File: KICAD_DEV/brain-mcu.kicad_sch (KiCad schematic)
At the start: 5 parts, among them U1 STM32H757IITx

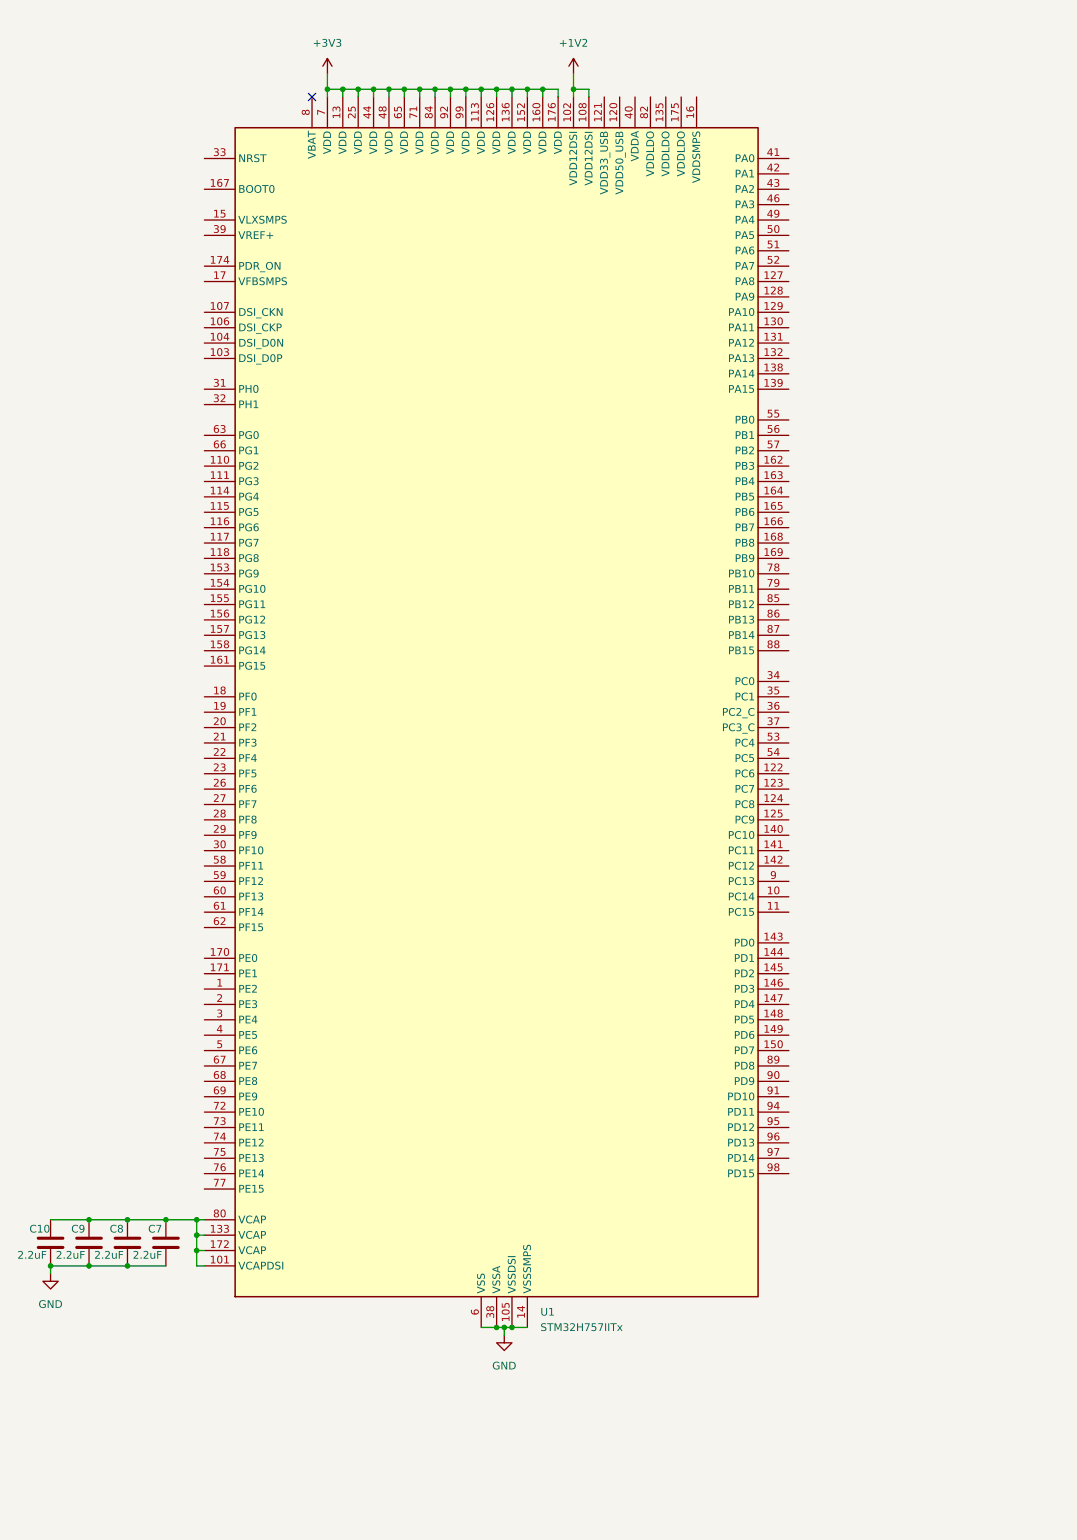
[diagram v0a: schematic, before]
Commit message: some decoupling and organization
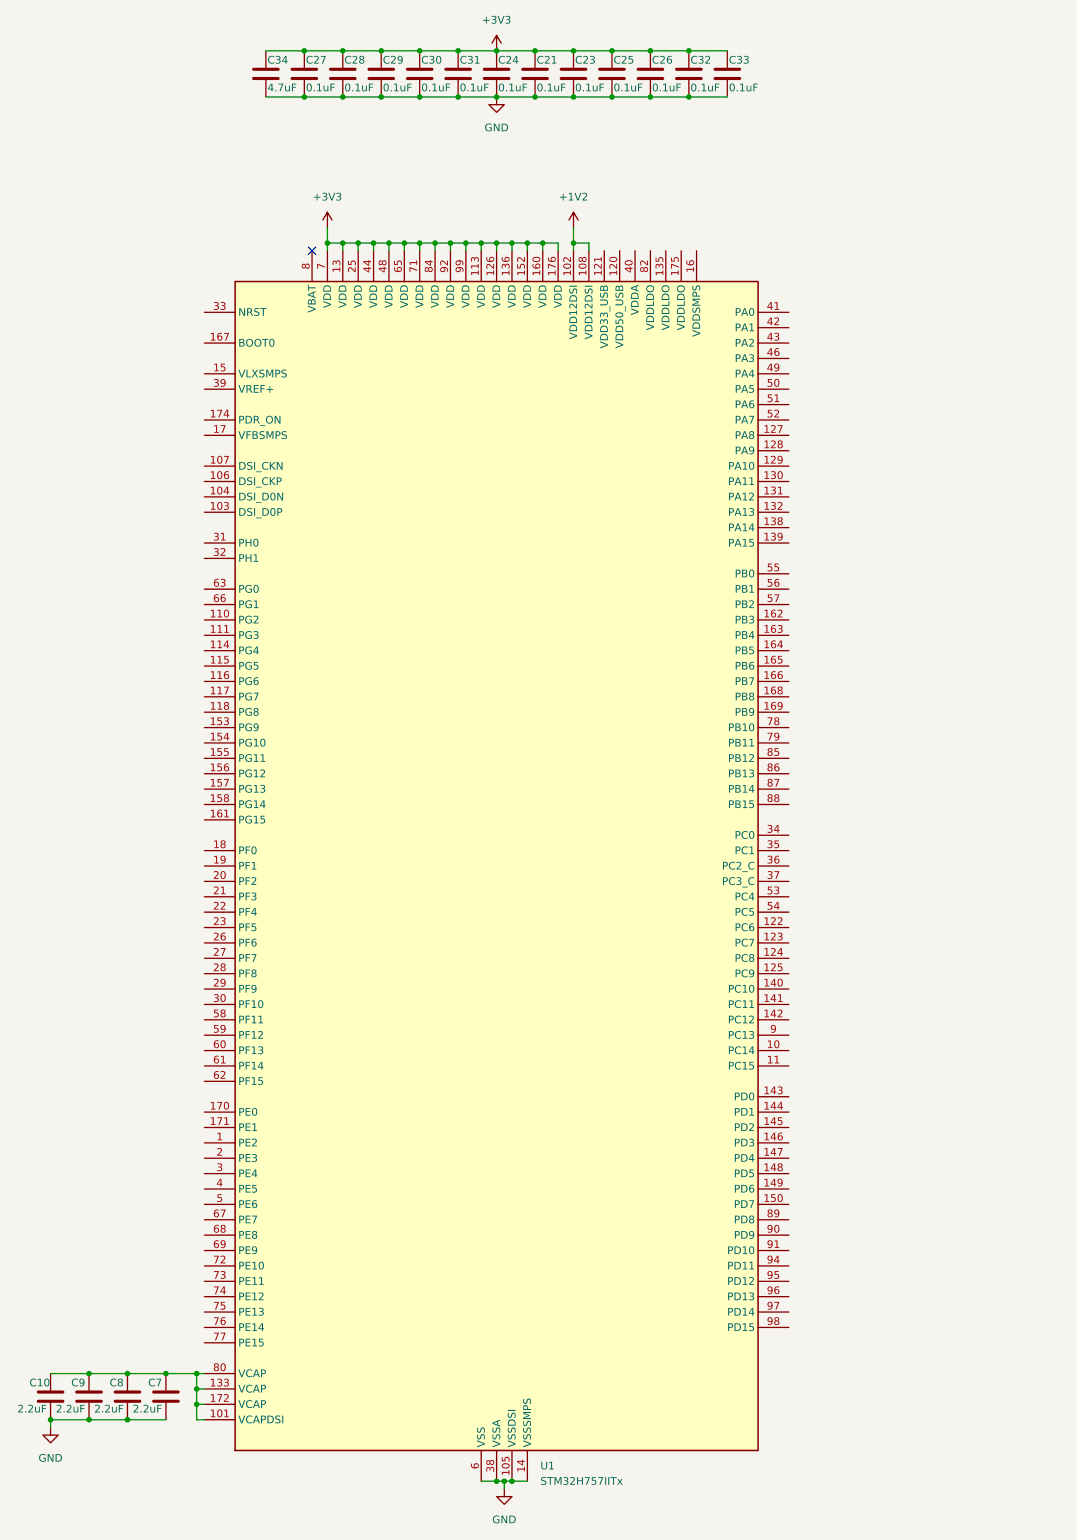
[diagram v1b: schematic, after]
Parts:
- added C21, C23, C24, C25, C26, C27, C28, C29, C30, C31, C32, C33: 0.1uF, symbol Device:C
- added C34: 4.7uF, symbol Device:C
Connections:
- net +3V3: now also C21.1, C23.1, C24.1, C25.1, C26.1, C27.1, C28.1, C29.1, C30.1, C31.1, C32.1, C33.1, C34.1
- net GND: now also C21.2, C23.2, C24.2, C25.2, C26.2, C27.2, C28.2, C29.2, C30.2, C31.2, C32.2, C33.2, C34.2
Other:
- moved on the sheet: C10, C7, C8, C9, U1

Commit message: changing the MCU for more chaos
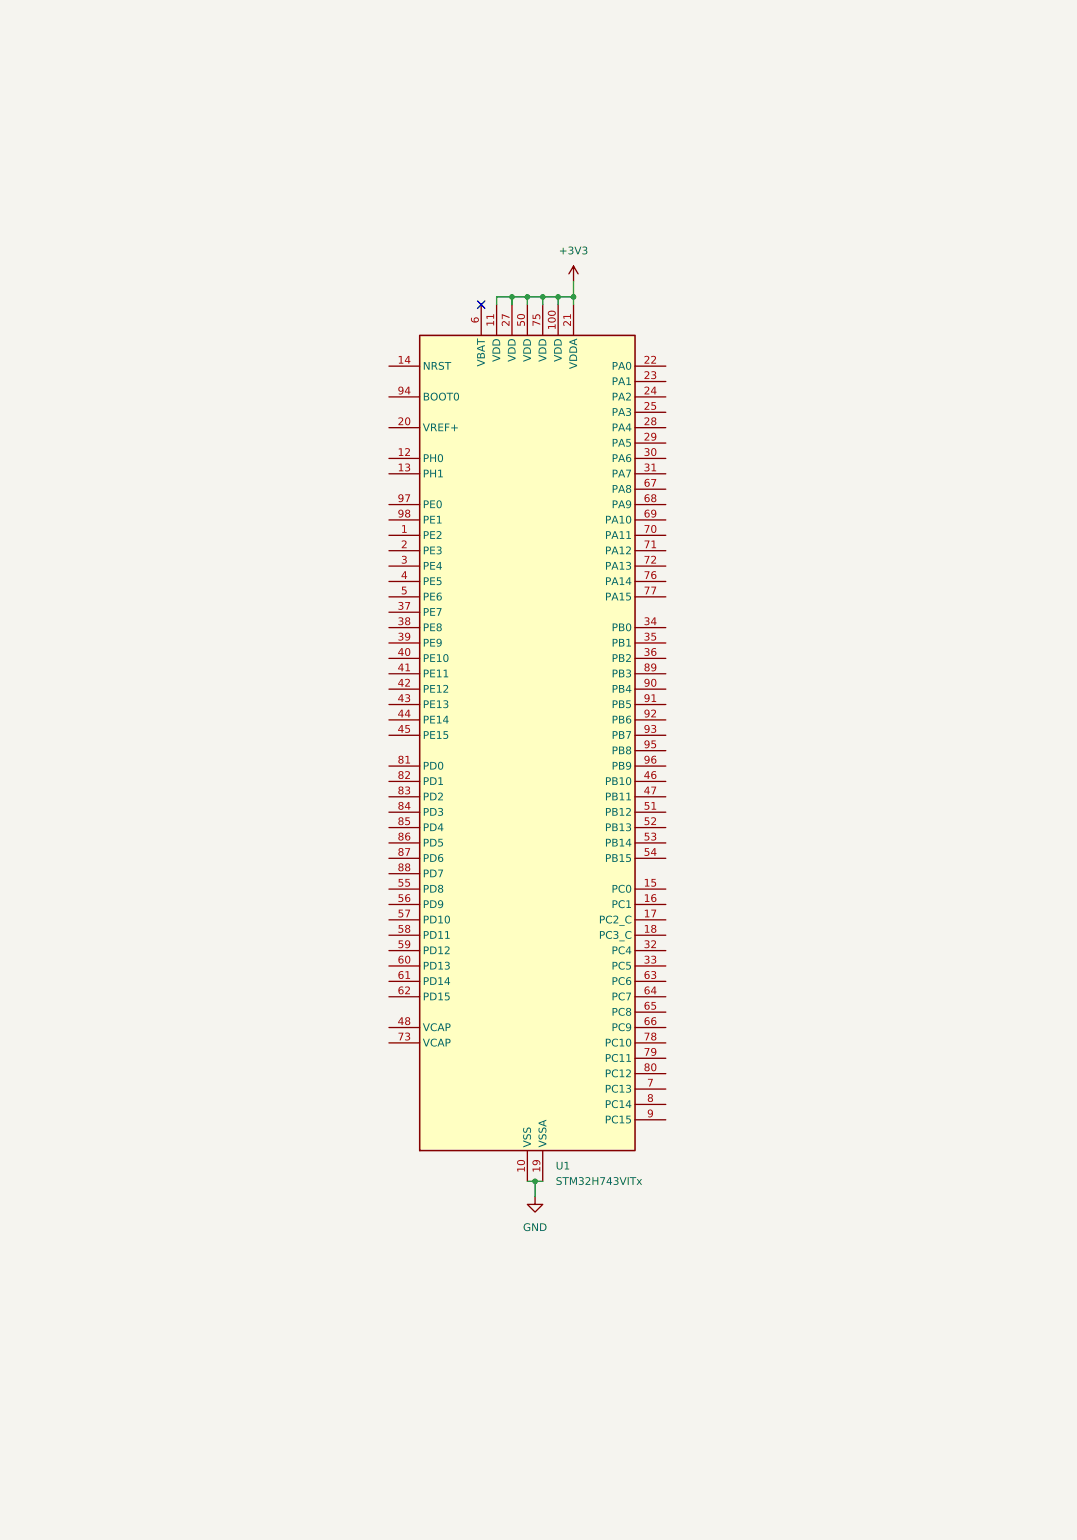
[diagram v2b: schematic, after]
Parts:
- removed C10, C7, C8, C9: 2.2uF, symbol Device:C
- removed C21, C23, C24, C25, C26, C27, C28, C29, C30, C31, C32, C33: 0.1uF, symbol Device:C
- removed C34: 4.7uF, symbol Device:C
- removed U1: STM32H757IITx, Package_QFP:LQFP-176_24x24mm_P0.5mm, symbol MCU_ST_STM32H7:STM32H757IITx
- added U1: STM32H743VITx, Package_QFP:LQFP-100_14x14mm_P0.5mm, symbol MCU_ST_STM32H7:STM32H743VITx
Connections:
- net +3V3: now also U1.100 (VDD), U1.11 (VDD), U1.21 (VDDA), U1.27 (VDD), U1.50 (VDD), U1.75 (VDD)
- net GND: now also U1.10 (VSS), U1.19 (VSSA), U1.26 (VSS), U1.49 (VSS), U1.74 (VSS), U1.99 (VSS)

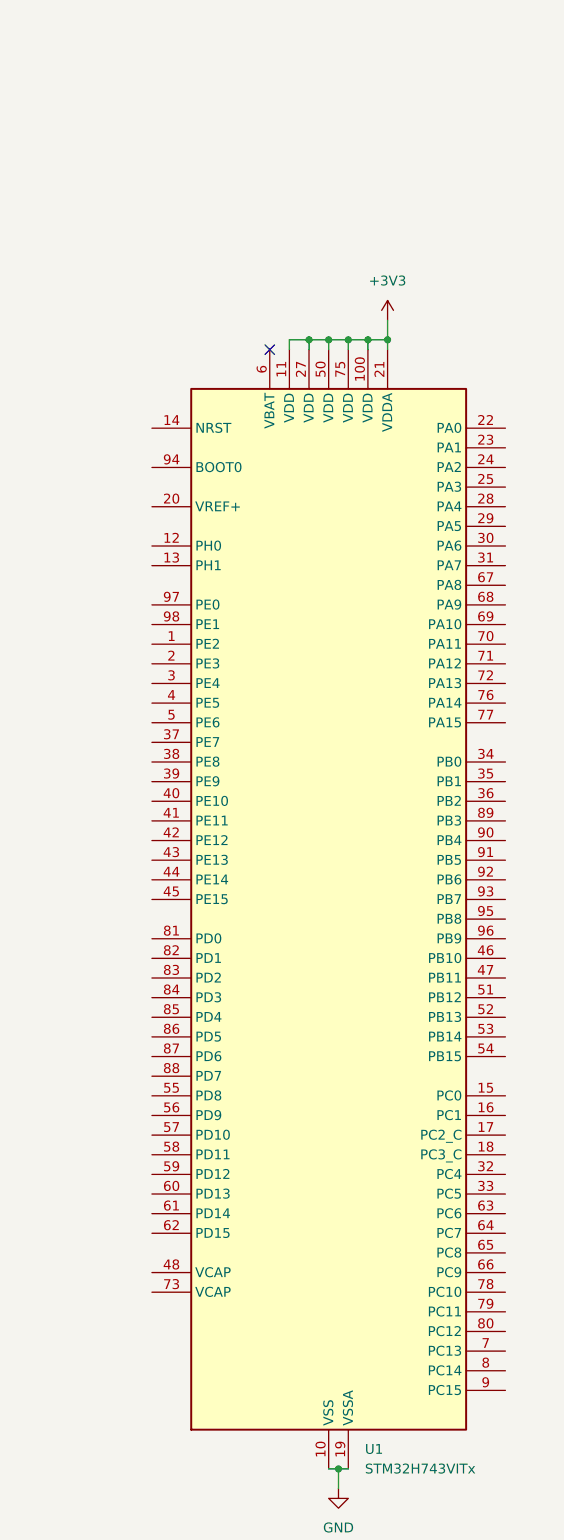
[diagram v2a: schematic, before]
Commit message: decoupling caps, vref, and vcap
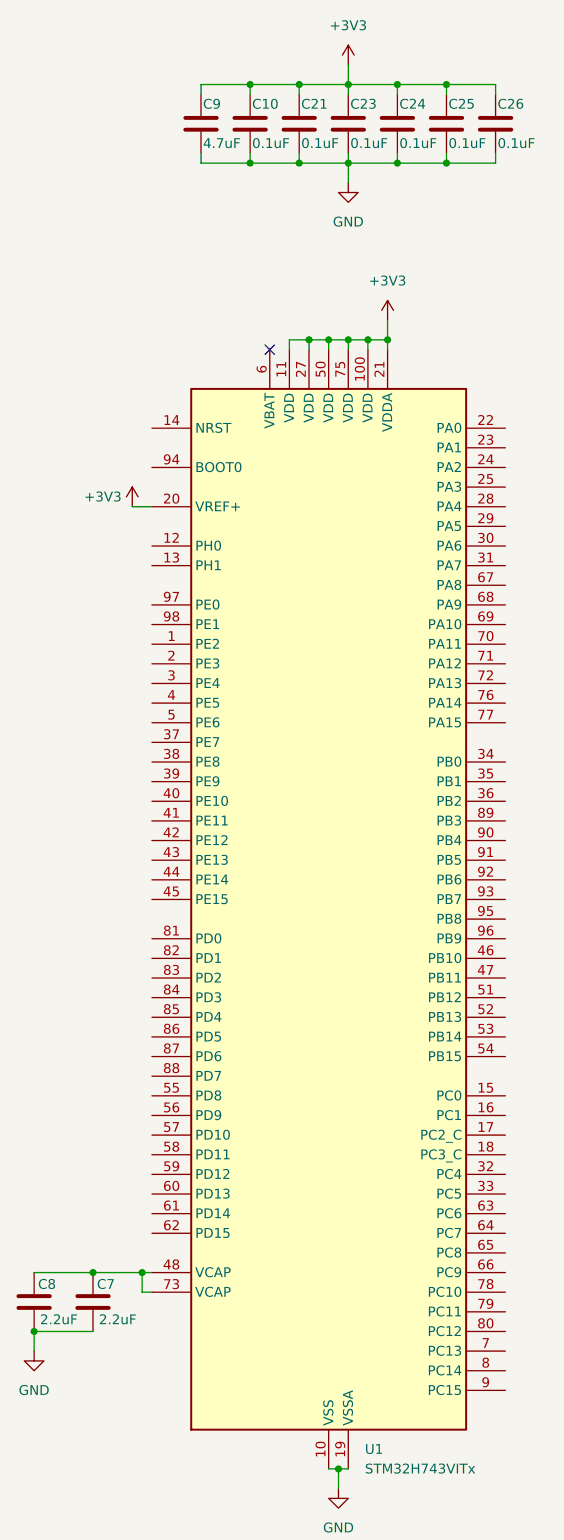
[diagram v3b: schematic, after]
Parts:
- added C10, C21, C23, C24, C25, C26: 0.1uF, symbol Device:C
- added C7, C8: 2.2uF, symbol Device:C
- added C9: 4.7uF, symbol Device:C
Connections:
- net +3V3: now also U1.20 (VREF+), C10.1, C21.1, C23.1, C24.1, C25.1, C26.1, C9.1
- net GND: now also C10.2, C21.2, C23.2, C24.2, C25.2, C26.2, C7.2, C8.2, C9.2
- net at U1.48 (VCAP): now also U1.73 (VCAP), C7.1, C8.1

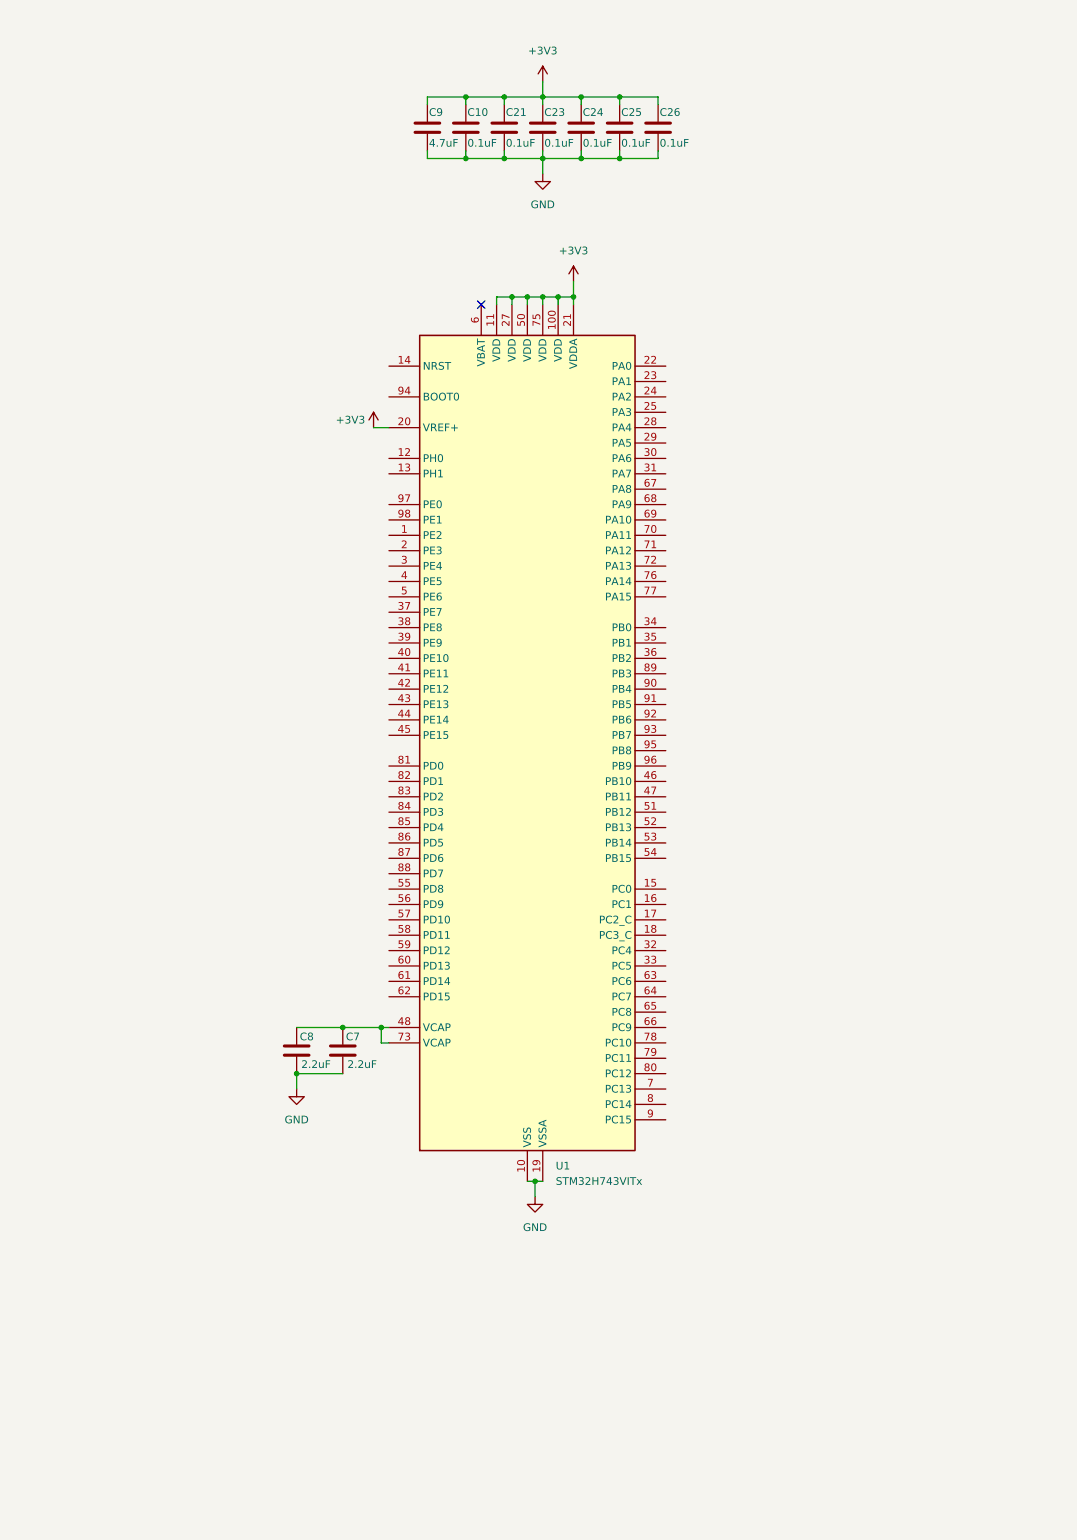
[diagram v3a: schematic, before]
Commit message: NRST and cleaner schematic
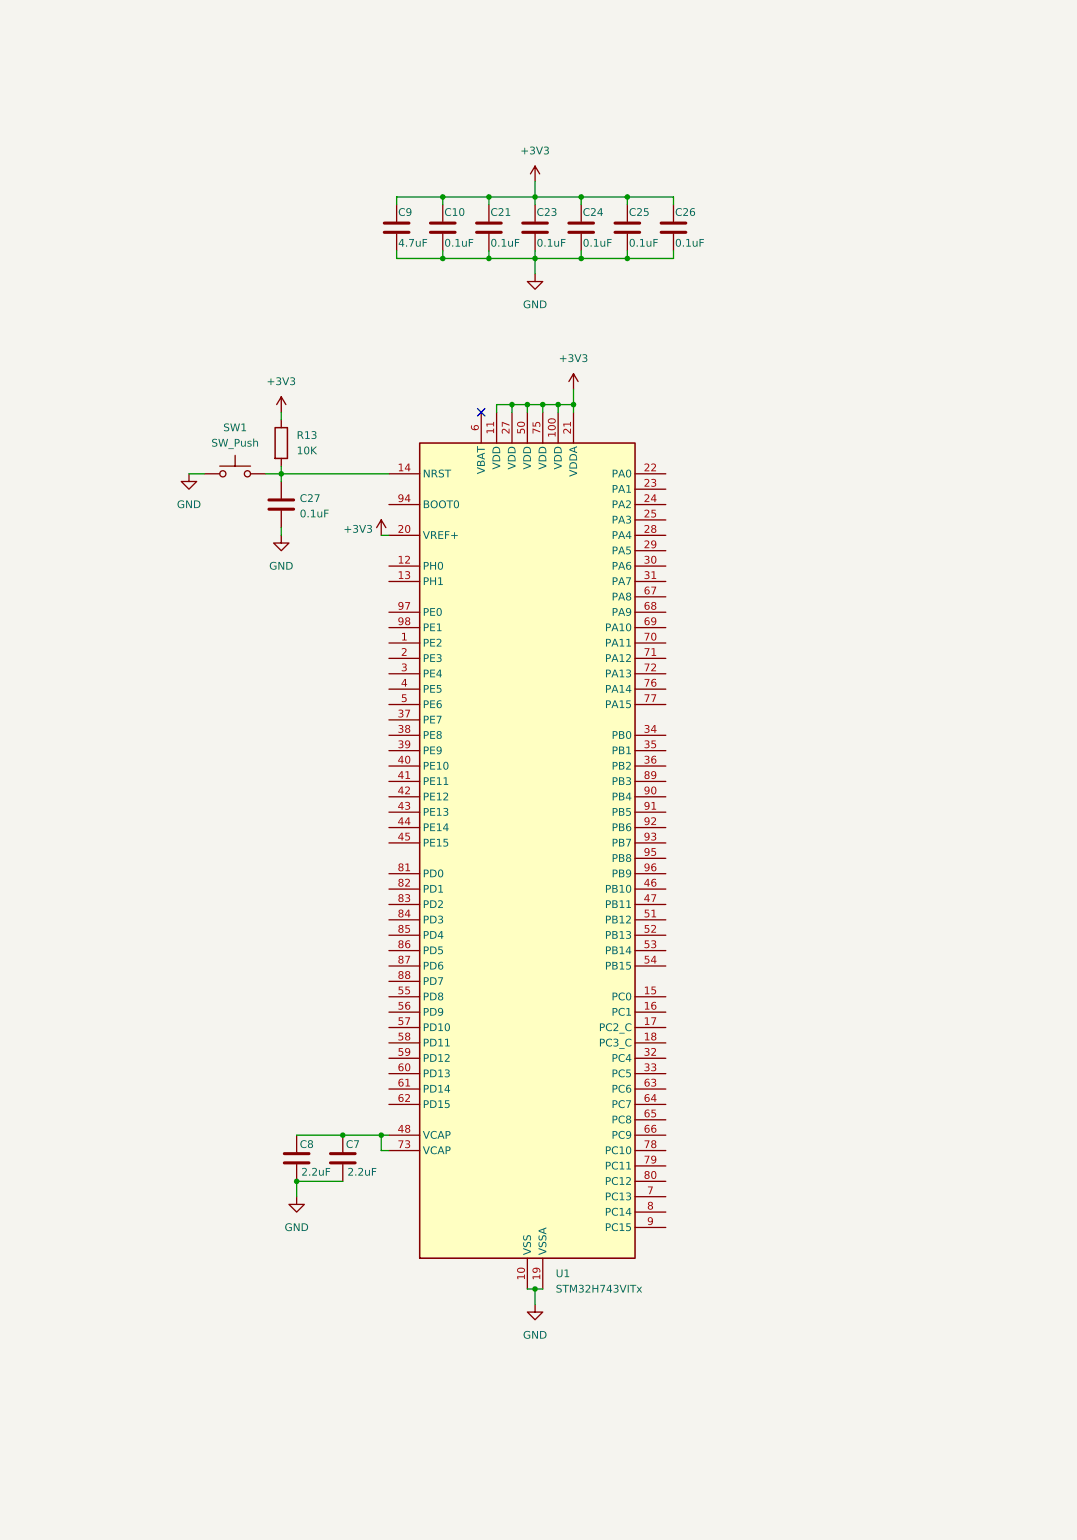
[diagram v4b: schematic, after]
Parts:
- added C27: 0.1uF, symbol Device:C
- added R13: 10K, symbol Device:R
- added SW1: SW_Push, symbol Switch:SW_Push
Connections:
- net +3V3: now also R13.1
- net GND: now also C27.2, SW1.1
- net at U1.14 (NRST): now also C27.1, R13.2, SW1.2
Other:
- moved on the sheet: C10, C21, C23, C24, C25, C26, C7, C8, C9, U1

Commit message: more cleaning up and adding boot
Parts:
- added R14: 10K, symbol Device:R
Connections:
- net GND: now also R14.2
- net RESET: now reaches C27.1, R13.2, SW1.2, U1.14 (NRST)
- net at U1.94 (BOOT0): now also R14.1
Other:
- note added: "USER FLASH >"
- moved on the sheet: C27, R13, SW1
